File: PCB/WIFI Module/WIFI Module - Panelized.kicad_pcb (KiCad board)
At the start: 4 copper layers, 60 x 65 mm, 144 parts, among them J1 Conn_01x01_Shielded, J2 Conn_02x04, U1 ESP8684, Y1 Q22FA12800230

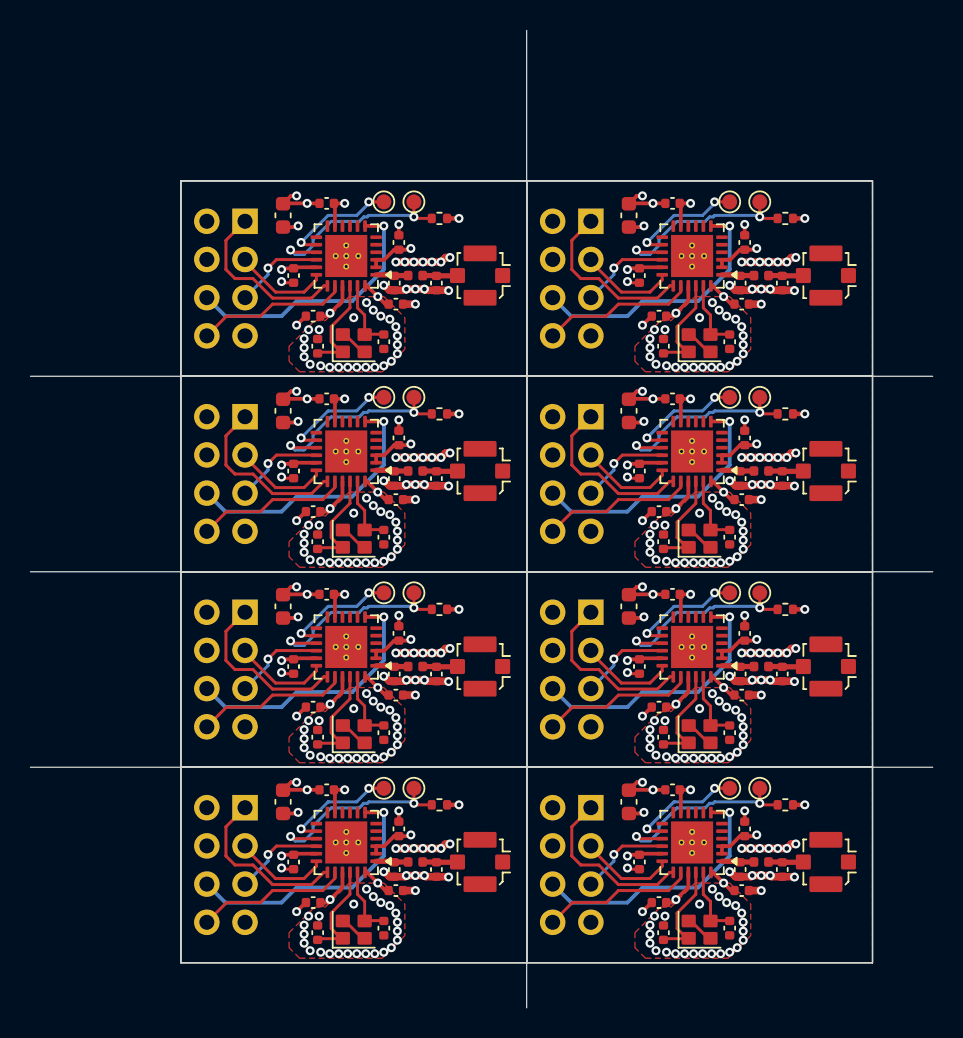
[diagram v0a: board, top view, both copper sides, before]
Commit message: Fixed allot of PCB mistakes and added more silkscreen
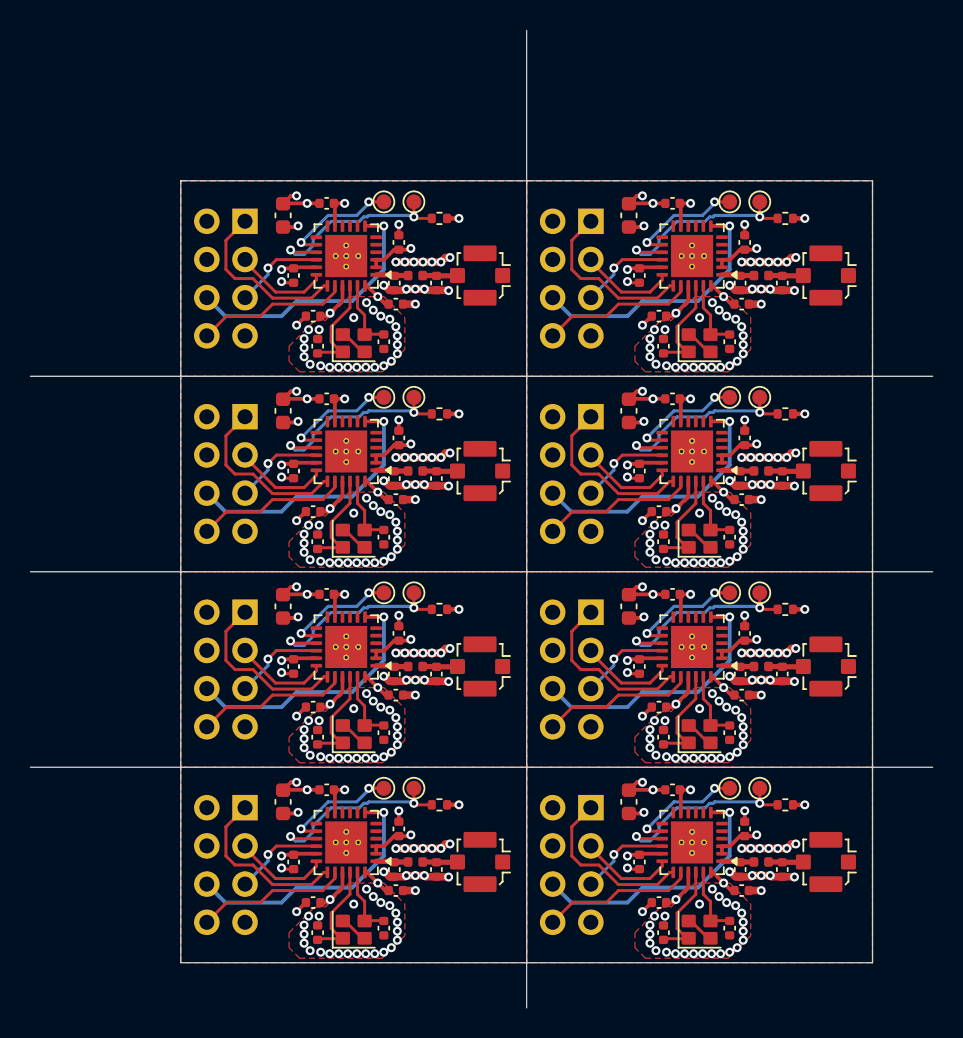
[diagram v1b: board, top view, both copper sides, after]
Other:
- outline, holes or cut-outs redrawn
